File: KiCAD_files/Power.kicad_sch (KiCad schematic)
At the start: 72 parts, among them J101 2604-1102, J102 2604-1102, J103 2604-1102, J104 2604-1102, J105 2604-1102, U101 AMC1311, U102 OPA316, U103 OPA316, U104 +-20A

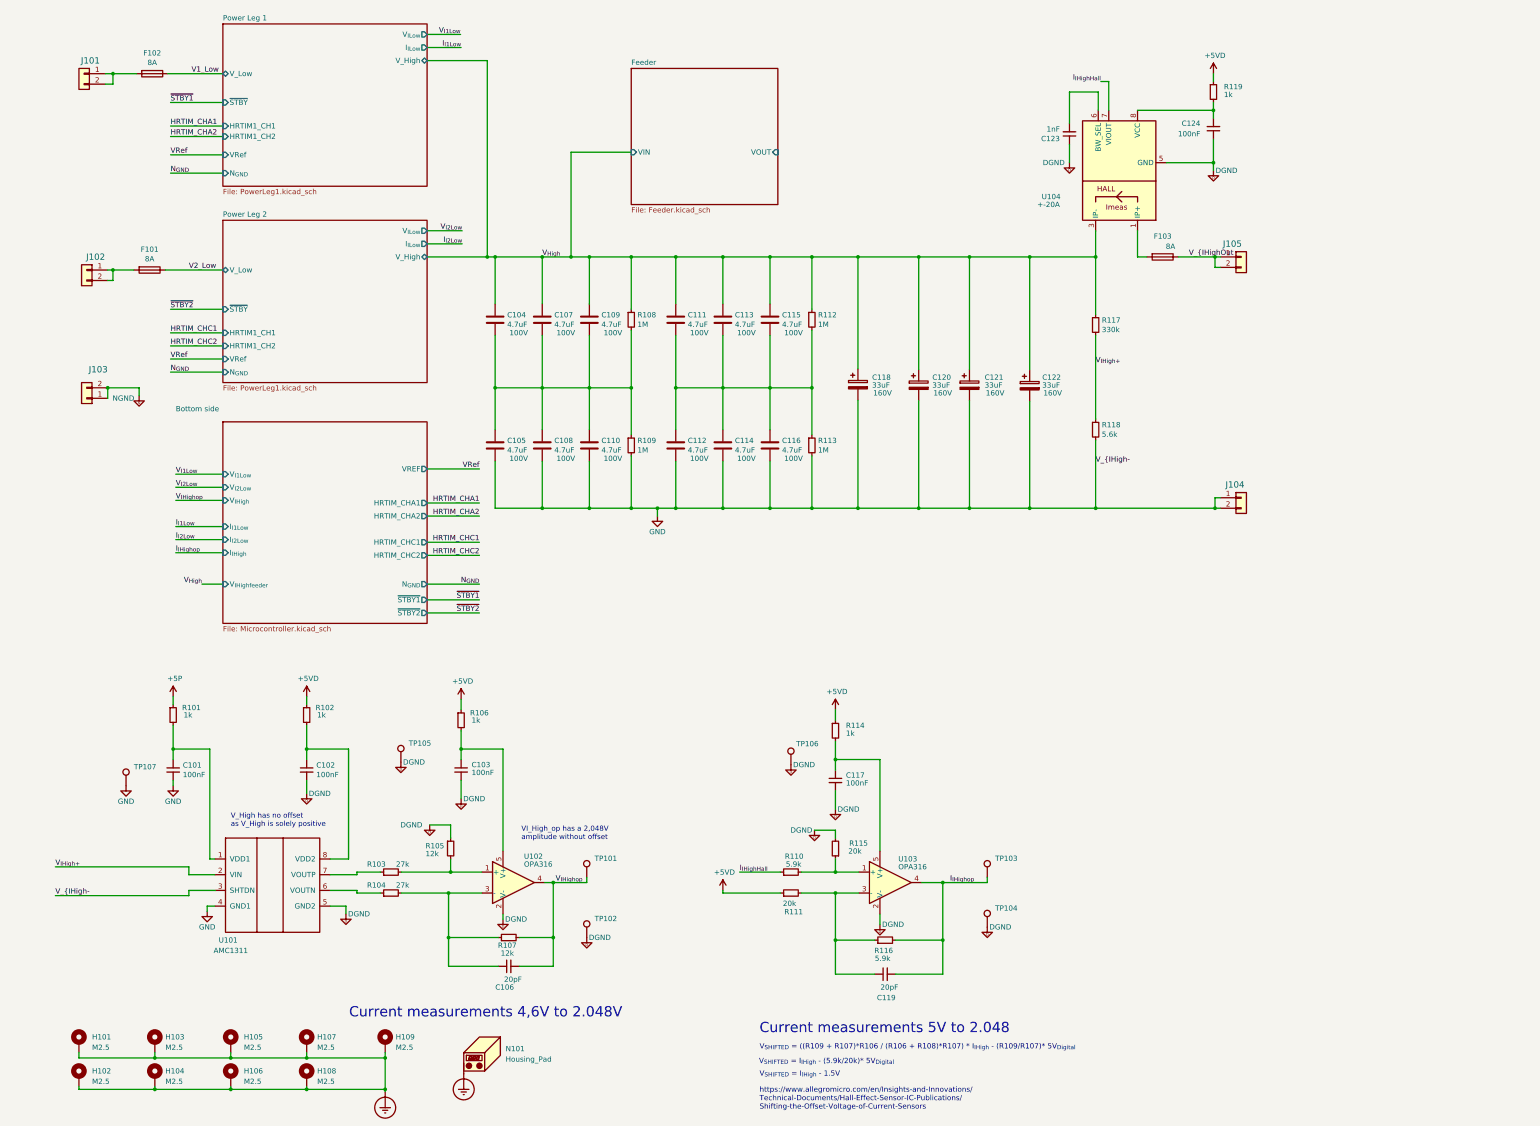
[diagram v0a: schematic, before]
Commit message: Closed open issues on TWIST V1.2. Cleaned the schematic and tweaked the routing files
Signed-off-by: Jean Alinei <jean.alinei@laas.fr>
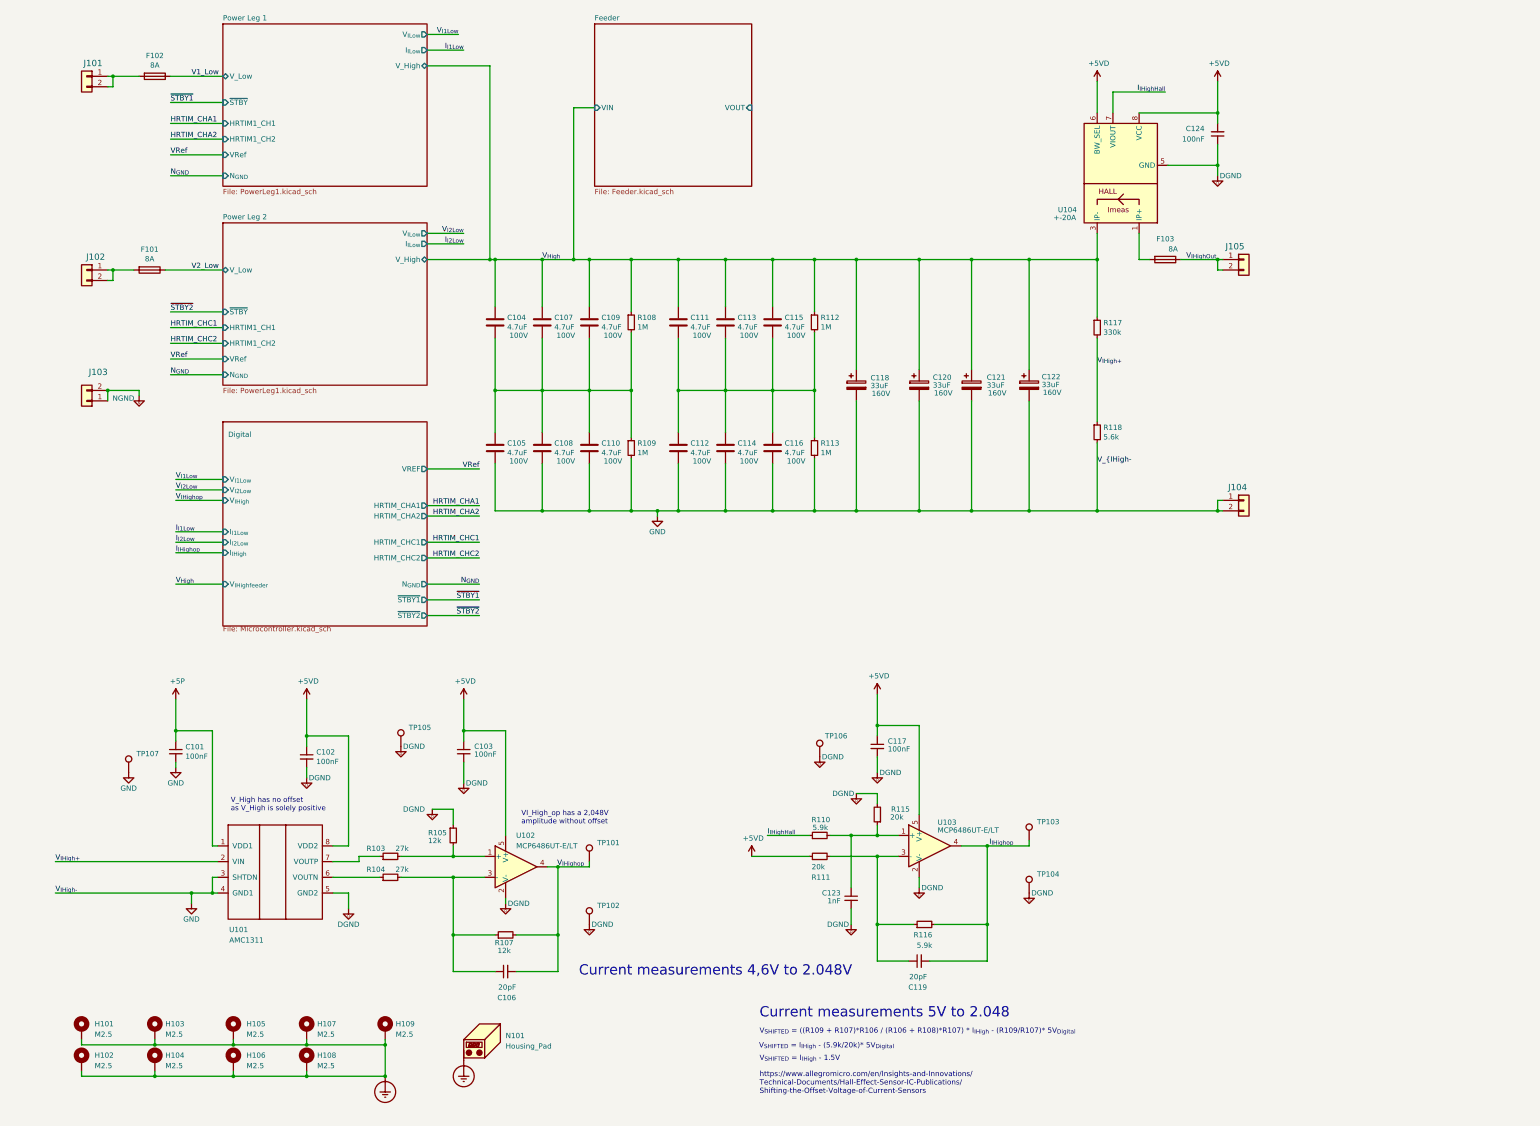
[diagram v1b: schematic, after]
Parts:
- removed R101, R102, R106, R114, R119: 1k, Footprints:R_0805_2012Metric, symbol Device:R_Small
- C123: #manf CL21C102JCFNNNE -> (none); Manf# CL21C102JCFNNNE -> C0805C104K5RACTU; manf# 885382207004 -> CC0805KRX7R9BB104
- U102, U103: value OPA316 -> MCP6486UT-E/LT
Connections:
- net +5P: now also C101.1, U101.1 (VDD1)
- net +5VD: now also C102.1, C103.1, C117.1, C124.2, U101.8 (VDD2), U102.5 (V+), U103.5 (V+), U104.6 (BW_SEL), U104.8 (VCC)
- net DGND: now also C123.2; no longer C123.1
- net at R110.2, R115.1, U103.1 (+): now also C123.1
- net V_{IHighOut renamed V_{IHighOut}
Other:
- sheet Bottom side renamed Digital
- moved on the sheet: C101, C102, C103, C104, C105, C106, C107, C108, C109, C110, C111, C112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

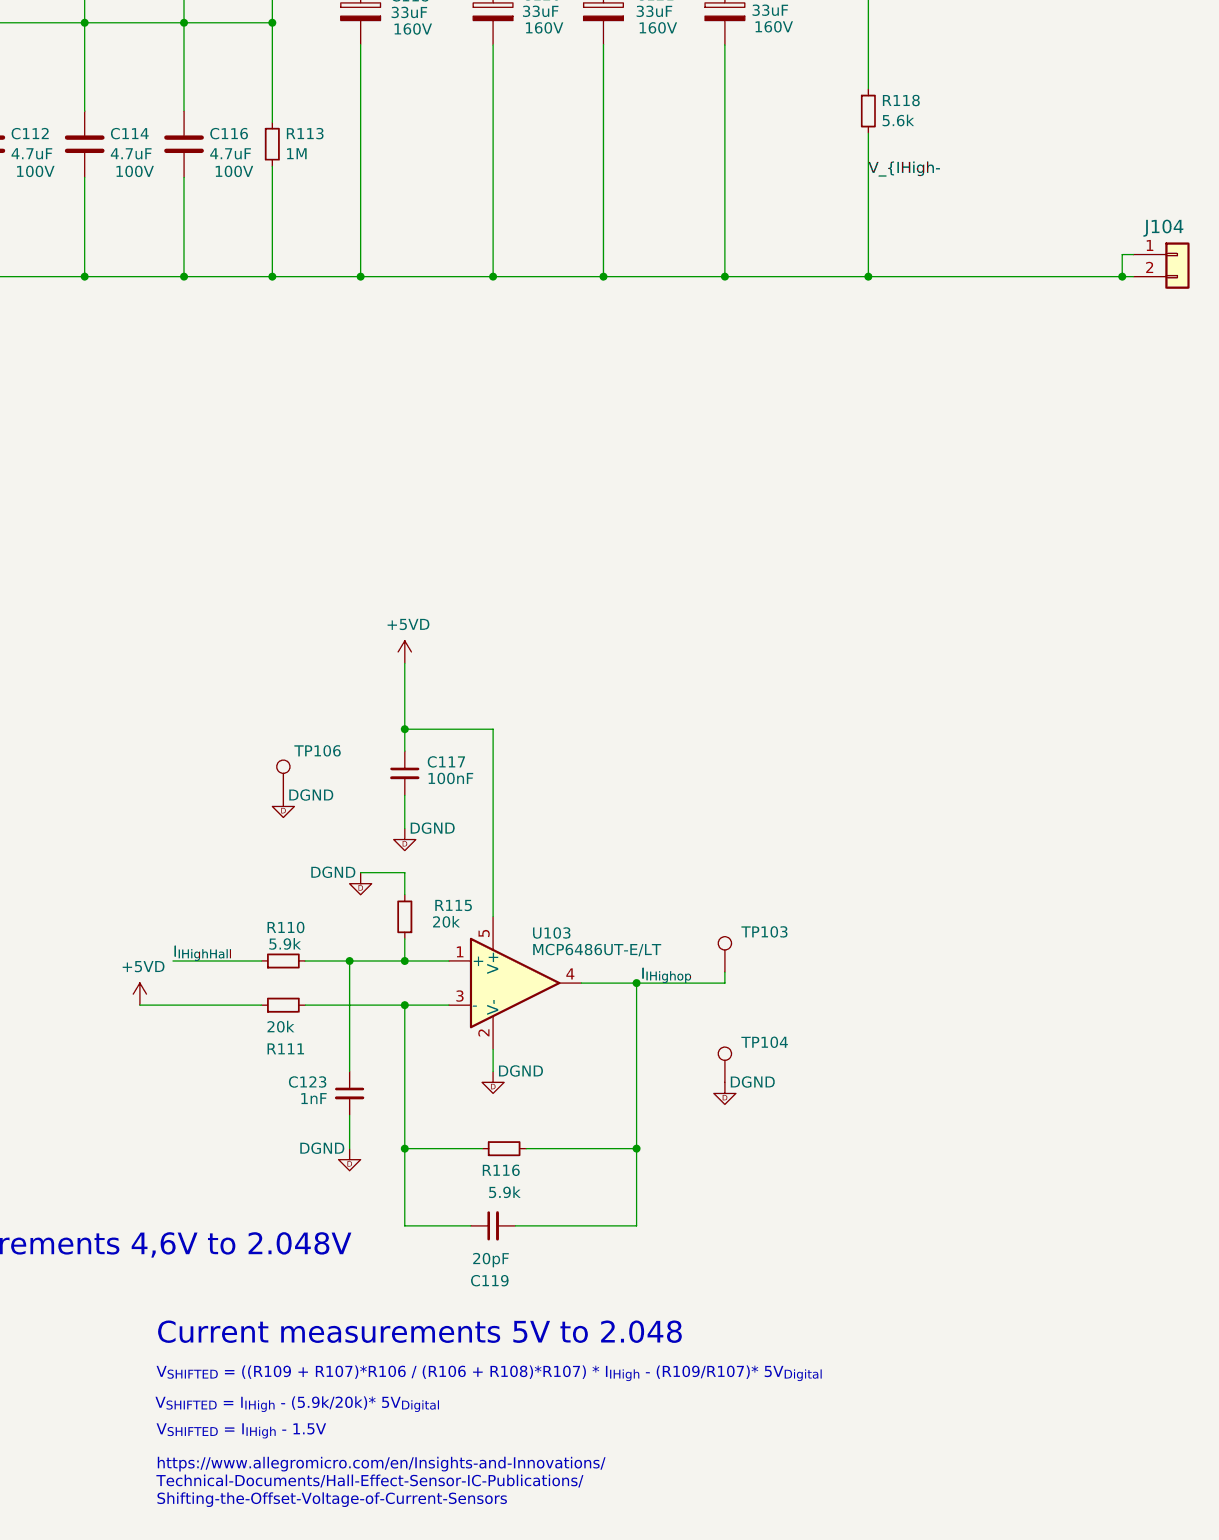
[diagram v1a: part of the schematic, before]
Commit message: Double check of each issue. Issue are now closed for V1.3
Signed-off-by: Jean Alinei <jean.alinei@laas.fr>
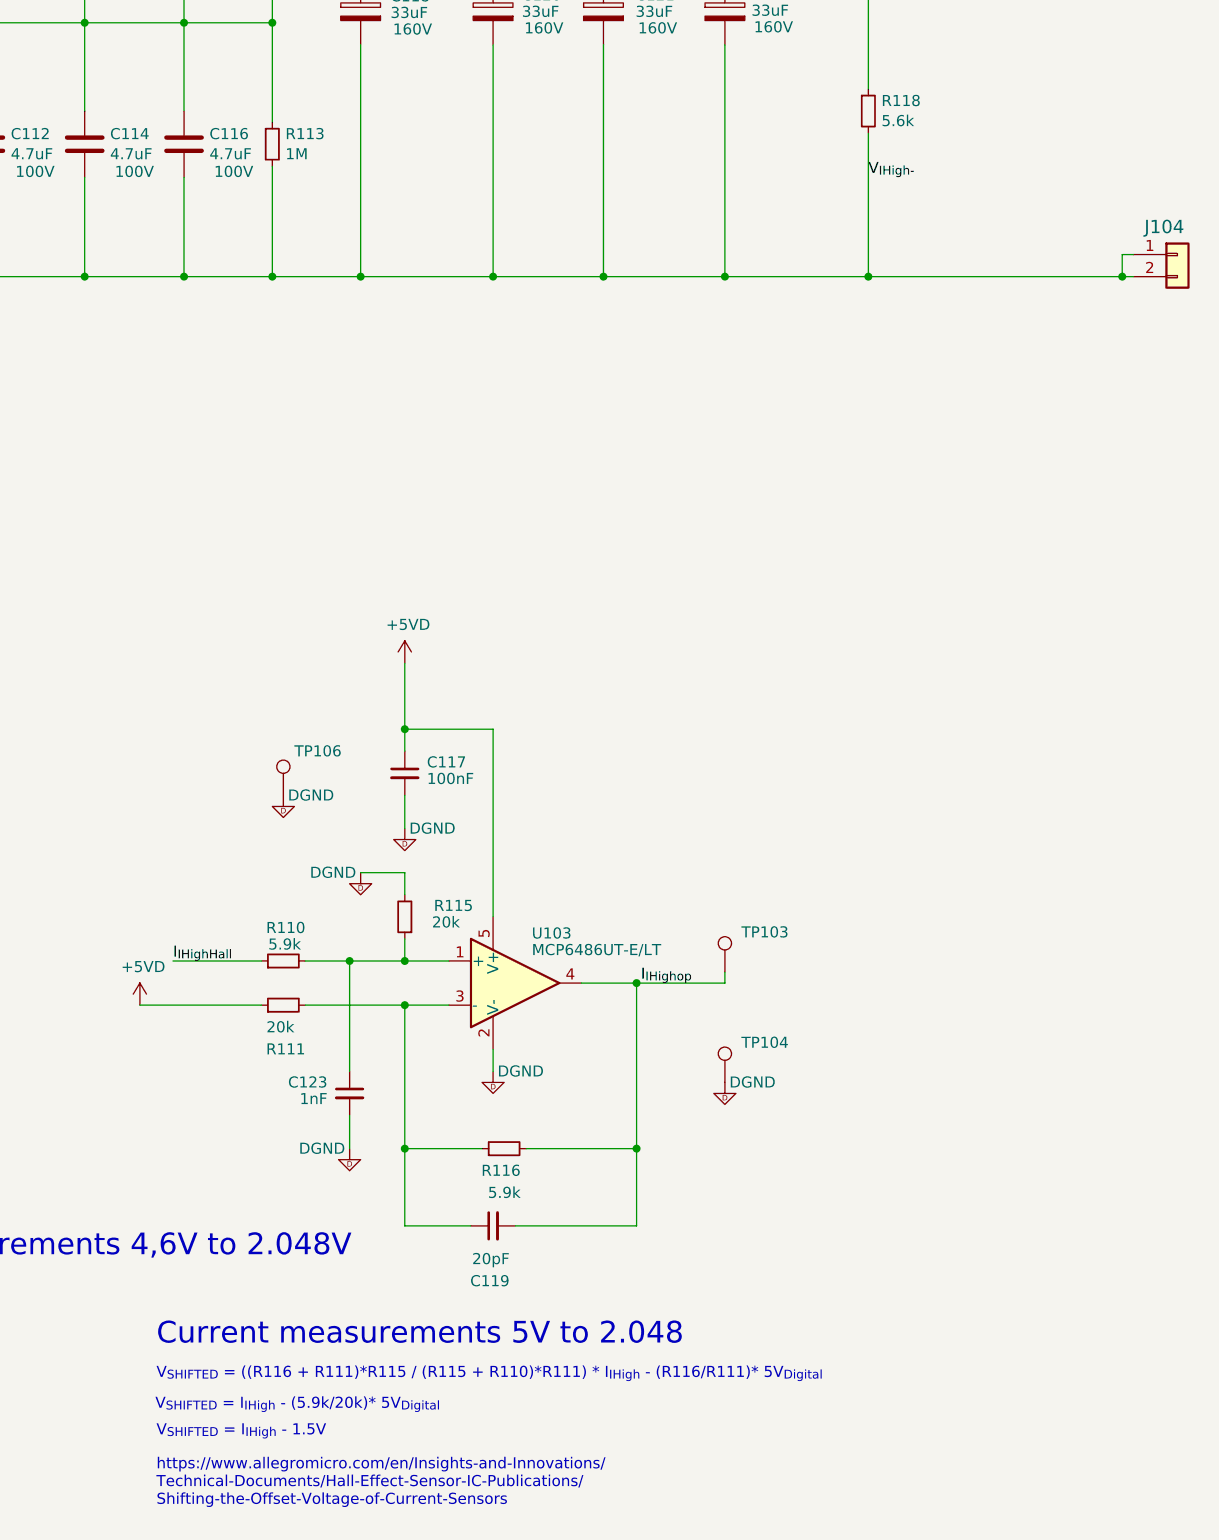
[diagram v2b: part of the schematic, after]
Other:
- note added: "V_{SHIFTED} = ((R116 + R111)*R115 / (R115 + R110)*R111) * I_{IHigh} - (R116/R111)* 5V_{Digital}"
- note removed: "V_{SHIFTED} = ((R109 + R107)*R106 / (R106 + R108)*R107) * I_{IHigh} - (R109/R107)* 5V_{Digital}"
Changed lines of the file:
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@@
     (effects (font (size 2.4892 2.4892)) (justify left bottom))
   )
-  (text "V_{SHIFTED} = ((R109 + R107)*R106 / (R106 + R108)*R107) * I_{IHigh} - (R109/R107)* 5V_{Digital}"
+  (text "V_{SHIFTED} = ((R116 + R111)*R115 / (R115 + R110)*R111) * I_{IHigh} - (R116/R111)* 5V_{Digital}"
     (at 203.835 262.89 0)
     (effects (font (size 1.27 1.27)) (justify left bottom))
@@
     (effects (font (size 1.27 1.27)) (justify left bottom))
   )
-  (label "V_{IHigh-" (at 285.75 124.46 0) (fields_autoplaced)
+  (label "V_{IHigh-}" (at 285.75 124.46 0) (fields_autoplaced)
     (effects (font (size 1.27 1.27)) (justify left bottom))
   )

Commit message: Fixed mechanical issues with front plate and corrected guard ring footprint. General position of the routing is now correctly aligned with 1mm grid.
Signed-off-by: Jean Alinei <jean.alinei@laas.fr>
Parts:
- U102, U103: footprint Package_TO_SOT_SMD:SOT-353_SC-70-5 -> Package_TO_SOT_SMD:SOT-353_SC-70-5_Handsoldering
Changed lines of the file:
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@@
       (effects (font (size 1.27 1.27)) (justify left))
     )
-    (property "Footprint" "Package_TO_SOT_SMD:SOT-353_SC-70-5" (at 247.65 217.17 0)
+    (property "Footprint" "Package_TO_SOT_SMD:SOT-353_SC-70-5_Handsoldering" (at 247.65 217.17 0)
       (effects (font (size 1.27 1.27)) hide)
     )
@@
       (effects (font (size 1.27 1.27)) (justify left))
     )
-    (property "Footprint" "Package_TO_SOT_SMD:SOT-353_SC-70-5" (at 147.32 222.25 0)
+    (property "Footprint" "Package_TO_SOT_SMD:SOT-353_SC-70-5_Handsoldering" (at 147.32 222.25 0)
       (effects (font (size 1.27 1.27)) hide)
     )
